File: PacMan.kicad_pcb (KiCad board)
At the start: 2 copper layers, 139.7 x 114.3 mm, 155 parts, among them J1 POWER+, J10 SEG2 CellMen, J11 BAL1, J12 BAL2, J13 AIR Left, J14 AIR Right, J15 SEG1, J16 SEG2, J2 POWER-, J3 TSV IN, J4 Charge Detection, J5 SEG1 CellMen, J6 BusBar Current Sensor, J7 Panel, J8 SLOOP, J9 GLV/CAN, K1 G5Q-1A4 DC24, K2 T9AS1D12-24, K3 T9AS1D12-24, Q1 DMN3730U, Q2 DMN3730U, Q4 DMP10H4D2S, Q5 DMP10H4D2S, U1 MCP9804, U10 LTC4151, U11 INA592, U12 MEF1S2405SP3C, U13 V7805-500, U14 Si8600AC, U15 Si8600AC, U16 TEC3-2419, U17 TEC3-2419, U18 AP2204K-5.0, U19 INA233, U2 TEC2-4815WI, U20 INA233, U3 ADM6320, U4 MCP2551-I-SN, U5 ESP32_DEVKITC, U6 MCP23008, U7 BQ32002, U8 ACHS-7122, U9 PDQE10-Q48-S24-D, Y1 RTC_32K

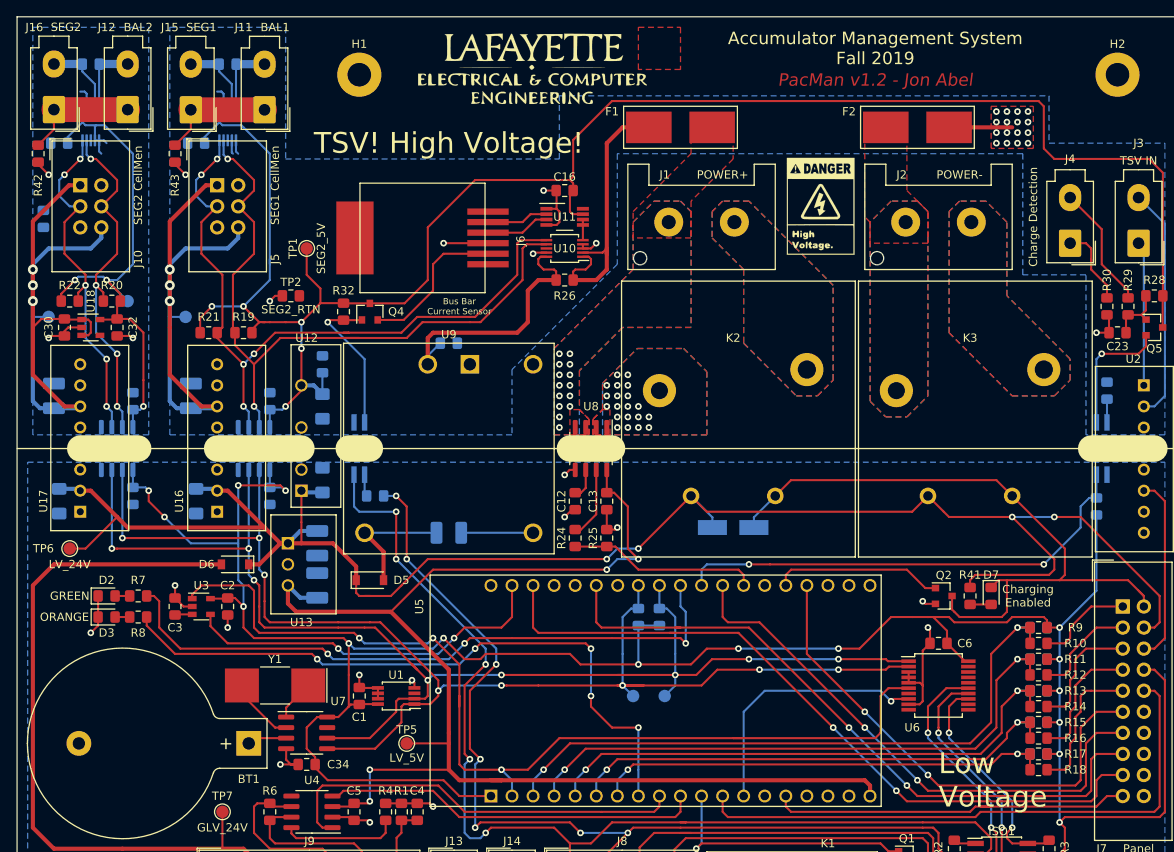
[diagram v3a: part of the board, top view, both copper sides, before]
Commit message: Added some planes around the balancing connectors and added the QRCode to the github page
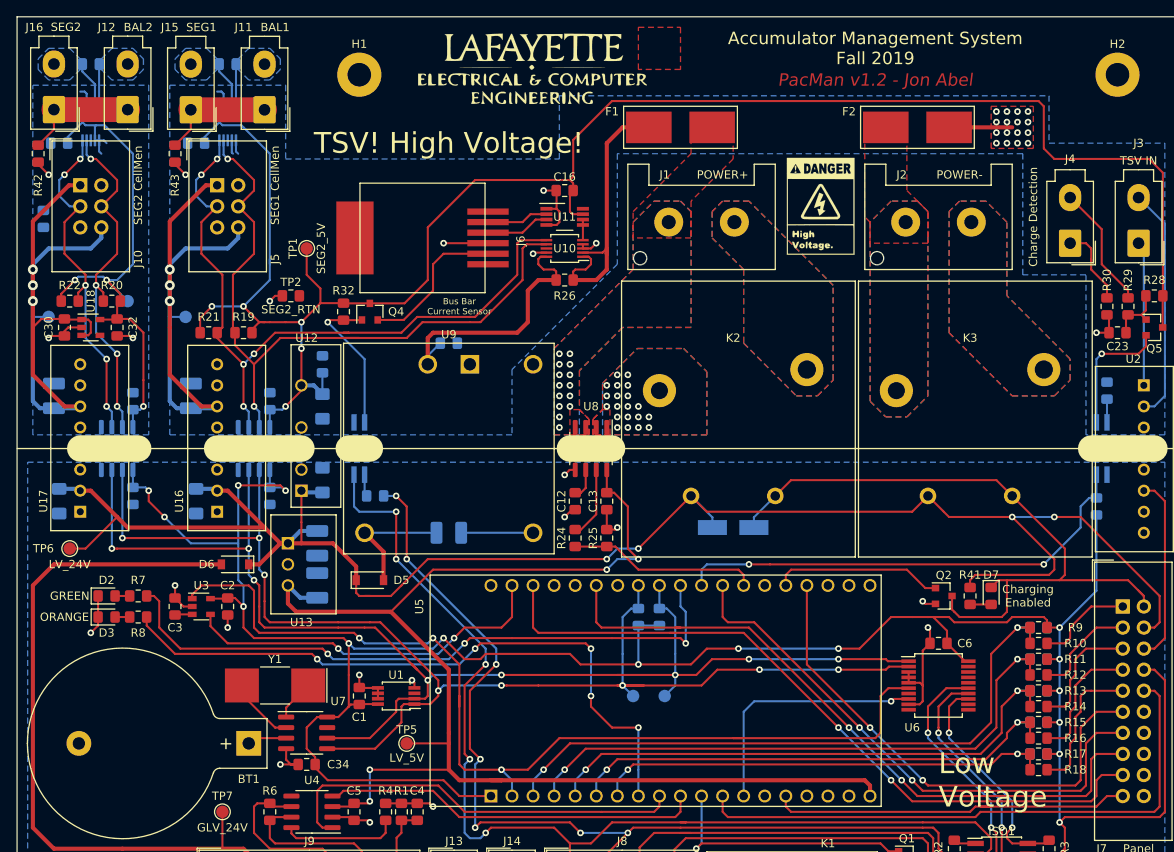
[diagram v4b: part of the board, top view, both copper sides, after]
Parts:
- added G***: LOGO, Lafayette_Electric_Car_Footprints:pacman_github_link, B.Cu at (144.1, 49.5)
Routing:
- net /BAL_SEG2+: track 11.6 -> 8.13 mm
- net /SEG2+: track 8.84 -> 5.42 mm
- net /SEG1+: track 8.84 -> 5.42 mm
- net /BAL_SEG1+: track 11.5 -> 8.13 mm
- net /MCU/IO_INT: track 31.7 -> 30.7 mm
- net /DISP_CS: track 60.3 -> 61.1 mm
- added copper zone on B.Cu, net /BAL_SEG1+
- added copper zone on B.Cu, net /BAL_SEG2+
- added copper zone on B.Cu, net /SEG1+
- added copper zone on B.Cu, net /SEG2+
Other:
- board text added: "Link to GitHub repository"

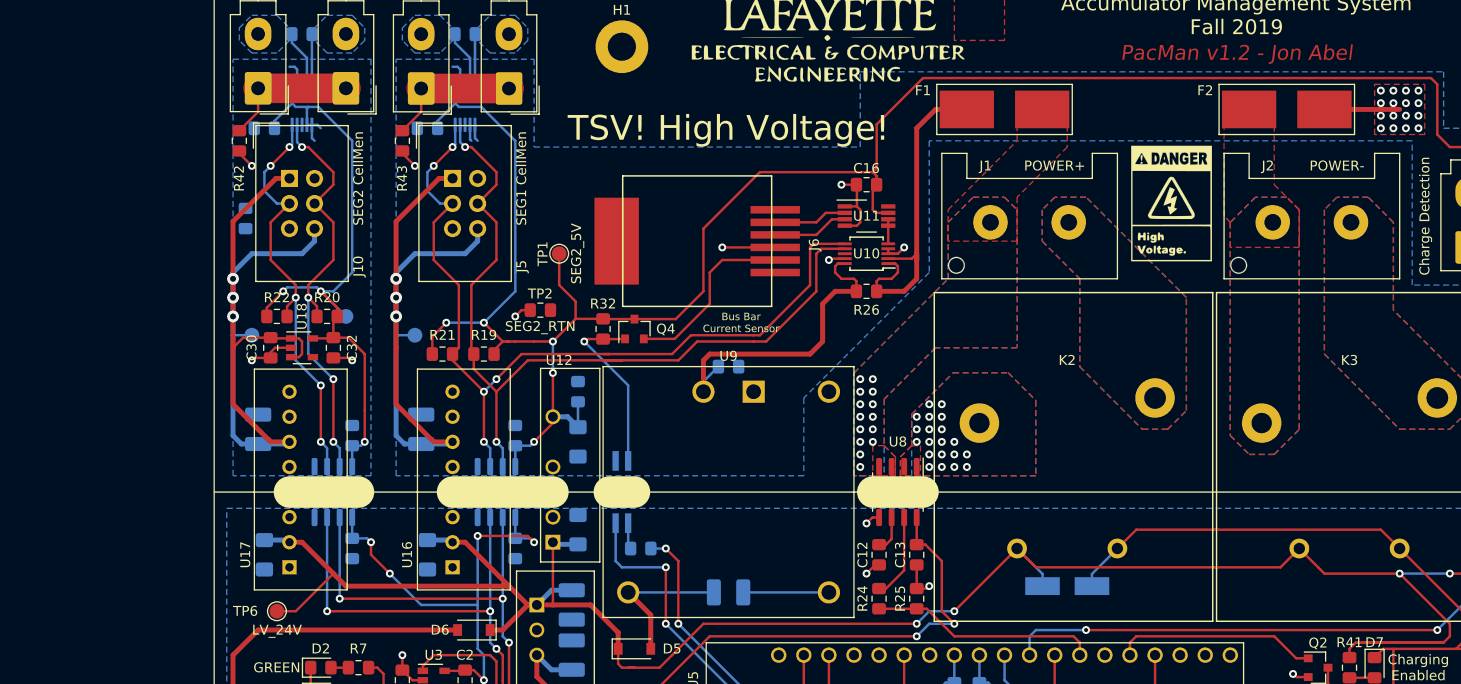
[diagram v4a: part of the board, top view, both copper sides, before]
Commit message: started re-routing for adjusted symmetric design
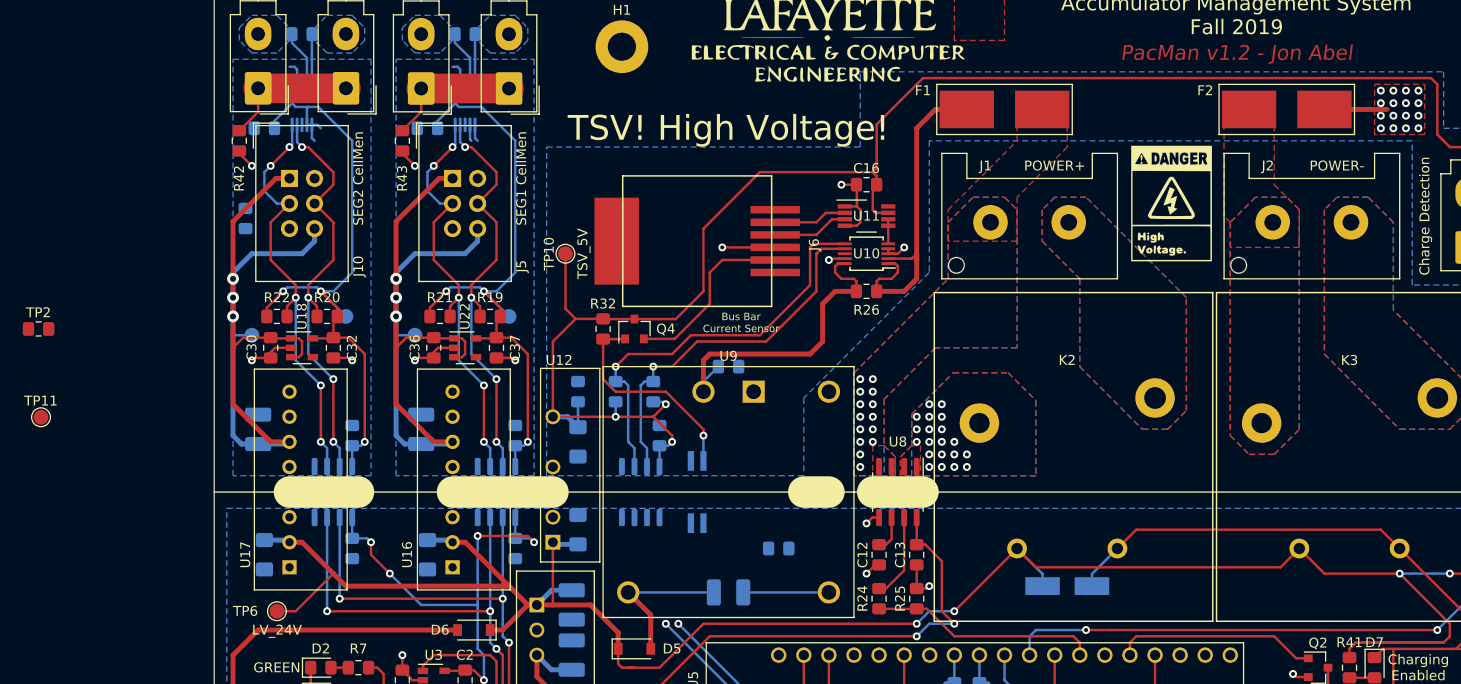
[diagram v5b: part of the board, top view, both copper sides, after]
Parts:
- removed G***: LOGO, Lafayette_Electric_Car_Footprints:pacman_github_link
- added C35: 0.1u/50V, Capacitor_SMD:C_0805_2012Metric_Pad1.15x1.40mm_HandSolder, B.Cu at (130.8, 83.2)
- added C36: 1u/50V, Capacitor_SMD:C_0805_2012Metric_Pad1.15x1.40mm_HandSolder, F.Cu at (108.0, 74.3)
- added C37: 2.2u/25V, Capacitor_SMD:C_0805_2012Metric_Pad1.15x1.40mm_HandSolder, F.Cu at (114.3, 74.3)
- added R44: 4.7k, Resistor_SMD:R_0805_2012Metric_Pad1.15x1.40mm_HandSolder, B.Cu at (130.2, 78.7)
- added R45: 4.7k, Resistor_SMD:R_0805_2012Metric_Pad1.15x1.40mm_HandSolder, B.Cu at (126.4, 78.7)
- added TP10: TSV_5V, TestPoint:TestPoint_Pad_D1.5mm, F.Cu at (121.3, 64.8)
- added TP11: TSV_RTN, TestPoint:TestPoint_Pad_D1.5mm, F.Cu at (68.2, 81.3)
- added U21: Si8600AC, Package_SO:SO-8_3.9x4.9mm_P1.27mm, B.Cu at (128.9, 88.9)
- added U22: AP2204K-5.0, Package_TO_SOT_SMD:SOT-23-5, F.Cu at (111.1, 74.3)
- TP1: moved to B.Cu
- moved TP2 50.8 mm to (67.9, 72.4)
- moved R35 14.0 mm to (142.9, 94.6)
- moved TP1 8.13 mm to (115.6, 71.1), turned to 270 degrees
- moved ISO4 7.62 mm to (134.6, 88.9)
- moved R19 3.86 mm to (113.7, 71.1)
- moved R21 3.82 mm to (108.6, 71.1)
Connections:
- C14 pad 2: /SEG1_RTN -> /PACK_RTN
- C16 pad 1: /SEG1_RTN -> /PACK_RTN
- C16 pad 2: /SEG1_5V -> /TSV_5V
- C23 pad 2: /SEG1_RTN -> /PACK_RTN
- C27 pad 1: /SEG1_5V -> /TSV_5V
- C27 pad 2: /SEG1_RTN -> /PACK_RTN
- F2 pad 2: /SEG1_RTN -> /PACK_RTN
- H1 pad 1: Net-(H1-Pad1) -> (no net)
- H2 pad 1: Net-(H2-Pad1) -> (no net)
- ISO4 pad 3: /SEG1_RTN -> /PACK_RTN
- J6 pad 1: Net-(J6-Pad1) -> (no net)
- J6 pad 4: /SEG1_RTN -> /PACK_RTN
- J6 pad 6: Net-(J6-Pad6) -> (no net)
- Q4 pad 3: /SEG1_5V -> /TSV_5V
- Q5 pad 3: /SEG1_5V -> /TSV_5V
- R28 pad 1: /SEG1_5V -> /TSV_5V
- R30 pad 1: /SEG1_RTN -> /PACK_RTN
- R31 pad 1: /SEG1_RTN -> /PACK_RTN
- R32 pad 1: /SEG1_5V -> /TSV_5V
- R34 pad 1: /SEG1_5V -> /TSV_5V
- R34 pad 2: /SEG1_RTN -> /PACK_RTN
- U1 pad 3: Net-(U1-Pad3) -> (no net)
- U10 pad 3: /SEG1_RTN -> /PACK_RTN
- U10 pad 4: /SEG1_RTN -> /PACK_RTN
- U10 pad 6: /SCL_SEG1 -> /SCL_TSV
- U10 pad 7: /SDA_SEG1 -> /SDA_TSV
- U10 pad 8: Net-(U10-Pad8) -> (no net)
- U10 pad 9: /SEG1_RTN -> /PACK_RTN
- U11 pad 1: /SEG1_RTN -> /PACK_RTN
- U11 pad 4: /SEG1_RTN -> /PACK_RTN
- U11 pad 7: /SEG1_5V -> /TSV_5V
- U11 pad 8: Net-(U11-Pad8) -> (no net)
- U12 pad 4: /SEG1_RTN -> /PACK_RTN
- U12 pad 6: /SEG1_5V -> /TSV_5V
- U16 pad 3: Net-(U16-Pad3) -> (no net)
- U17 pad 3: Net-(U17-Pad3) -> (no net)
- U18 pad 4: Net-(U18-Pad4) -> (no net)
- U19 pad 3: Net-(U19-Pad3) -> (no net)
- U2 pad 3: Net-(U2-Pad3) -> (no net)
- U20 pad 3: Net-(U20-Pad3) -> (no net)
- U4 pad 5: Net-(U4-Pad5) -> (no net)
- U5 pad 16: Net-(U5-Pad16) -> (no net)
- U5 pad 17: Net-(U5-Pad17) -> (no net)
- U5 pad 18: Net-(U5-Pad18) -> (no net)
- U5 pad 23: Net-(U5-Pad23) -> (no net)
- U5 pad 24: Net-(U5-Pad24) -> (no net)
- U5 pad 33: Net-(U5-Pad33) -> (no net)
- U5 pad 36: Net-(U5-Pad36) -> (no net)
- U5 pad 37: Net-(U5-Pad37) -> (no net)
- U5 pad 38: Net-(U5-Pad38) -> (no net)
- U6 pad 10: Net-(U6-Pad10) -> (no net)
- U6 pad 11: Net-(U6-Pad11) -> (no net)
- U6 pad 12: Net-(U6-Pad12) -> (no net)
- U6 pad 16: Net-(U6-Pad16) -> (no net)
- U6 pad 17: Net-(U6-Pad17) -> (no net)
- U6 pad 18: Net-(U6-Pad18) -> (no net)
- U6 pad 19: Net-(U6-Pad19) -> (no net)
- U6 pad 7: Net-(U6-Pad7) -> (no net)
- U7 pad 7: Net-(U7-Pad7) -> (no net)
- U9 pad 1: /SEG1_RTN -> /PACK_RTN
- U9 pad 6: Net-(U9-Pad6) -> (no net)
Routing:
- net /TSV_5V: track 0.00 -> 194.2 mm, vias 0 -> 3
- net /SEG1_5V: track 231.0 -> 65.3 mm, vias 5 -> 3
- net /SCL_SEG1: track 86.8 -> 43.0 mm
- net /SDA_SEG1: track 85.8 -> 42.7 mm, vias 2 -> 4
- net /SCL_TSV: track 0.00 -> 42.0 mm, vias 0 -> 1
- net /SDA_TSV: track 0.00 -> 38.0 mm, vias 0 -> 1
- net /PACK_RTN: track 0.00 -> 27.9 mm, vias 0 -> 21
- net /SEG1_RTN: track 38.5 -> 14.4 mm, vias 23 -> 3
- net /AIRS-: track 147.6 -> 132.7 mm, vias 5 -> 4
- net /SEG1_9V: track 68.7 -> 78.8 mm
- net /AIRS+: track 143.7 -> 134.1 mm, vias 7 -> 6
- net /Isolation/EN_AMPS: track 18.2 -> 21.8 mm
- net Net-(ISO4-Pad1): track 2.67 -> 0.00 mm
- added copper zone on B.Cu, net /PACK_RTN
- added copper zone on F.Cu, net /PACK_RTN
- removed copper zone on F.Cu, net /SEG1_RTN

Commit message: incremental work
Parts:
- TP1: value SEG2_5V -> SEG1_5V
- TP11: footprint TestPoint:TestPoint_Pad_D1.5mm -> Resistor_SMD:R_0805_2012Metric_Pad1.15x1.40mm_HandSolder
- TP2: value SEG2_RTN -> SEG1_RTN; moved to B.Cu
- moved TP11 59.5 mm to (122.3, 56.5), turned to 180 degrees
- moved TP2 39.1 mm to (105.4, 61.2), turned to 270 degrees
- moved R35 5.46 mm to (138.0, 92.1)
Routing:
- net /LV_3V3: track 312.4 -> 329.6 mm, vias 16 -> 19
- net /SCL_GLV: track 160.9 -> 168.1 mm, vias 8 -> 9
- net /SDA_GLV: track 163.1 -> 168.4 mm, vias 8 -> 9
- net Net-(ISO4-Pad1): track 0.00 -> 1.77 mm
- net /PACK_RTN: track 27.9 -> 29.7 mm, vias 21 -> 22
- net /LV_5V: track 163.8 -> 162.3 mm
- net /LV_24V: track 226.1 -> 227.2 mm

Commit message: Fixed a little bit of stuff
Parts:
- added G***: LOGO, Lafayette_Electric_Car_Footprints:pacman_github_link, B.Cu at (144.1, 50.2)
- moved Y1 0.64 mm to (116.8, 118.1)
- moved TP12 0.63 mm to (89.5, 73.7)
- moved TP3 0.63 mm to (106.0, 73.7)
- turned TP11 to 0 degrees
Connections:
- H1 pad 1: (no net) -> Net-(H1-Pad1)
- H2 pad 1: (no net) -> Net-(H2-Pad1)
- J6 pad 1: (no net) -> Net-(J6-Pad1)
- J6 pad 6: (no net) -> Net-(J6-Pad6)
- U1 pad 3: (no net) -> Net-(U1-Pad3)
- U10 pad 8: (no net) -> Net-(U10-Pad8)
- U11 pad 8: (no net) -> Net-(U11-Pad8)
- U16 pad 3: (no net) -> Net-(U16-Pad3)
- U17 pad 3: (no net) -> Net-(U17-Pad3)
- U18 pad 4: (no net) -> Net-(U18-Pad4)
- U19 pad 3: (no net) -> Net-(U19-Pad3)
- U2 pad 3: (no net) -> Net-(U2-Pad3)
- U20 pad 3: (no net) -> Net-(U20-Pad3)
- U22 pad 4: (no net) -> Net-(U22-Pad4)
- U4 pad 5: (no net) -> Net-(U4-Pad5)
- U5 pad 16: (no net) -> Net-(U5-Pad16)
- U5 pad 17: (no net) -> Net-(U5-Pad17)
- U5 pad 18: (no net) -> Net-(U5-Pad18)
- U5 pad 23: (no net) -> Net-(U5-Pad23)
- U5 pad 24: (no net) -> Net-(U5-Pad24)
- U5 pad 33: (no net) -> Net-(U5-Pad33)
- U5 pad 36: (no net) -> Net-(U5-Pad36)
- U5 pad 37: (no net) -> Net-(U5-Pad37)
- U5 pad 38: (no net) -> Net-(U5-Pad38)
- U6 pad 10: (no net) -> Net-(U6-Pad10)
- U6 pad 11: (no net) -> Net-(U6-Pad11)
- U6 pad 12: (no net) -> Net-(U6-Pad12)
- U6 pad 16: (no net) -> Net-(U6-Pad16)
- U6 pad 17: (no net) -> Net-(U6-Pad17)
- U6 pad 18: (no net) -> Net-(U6-Pad18)
- U6 pad 19: (no net) -> Net-(U6-Pad19)
- U6 pad 7: (no net) -> Net-(U6-Pad7)
- U7 pad 7: (no net) -> Net-(U7-Pad7)
- U9 pad 6: (no net) -> Net-(U9-Pad6)
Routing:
- net /SDA_GLV: track 168.4 -> 212.5 mm, vias 9 -> 12
- net /SCL_GLV: track 168.1 -> 209.6 mm, vias 9 -> 12
- net /AIRS+: track 134.1 -> 148.4 mm, vias 6 -> 7
- net /GLV_RTN: track 81.1 -> 94.4 mm
- net /AIRS-: track 132.7 -> 143.9 mm, vias 4 -> 5
- net Net-(U7-Pad2): track 8.07 -> 7.44 mm
